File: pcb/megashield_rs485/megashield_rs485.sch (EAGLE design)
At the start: 20 parts, among them J11 DYNAMIXEL_RS485, U1 RS485

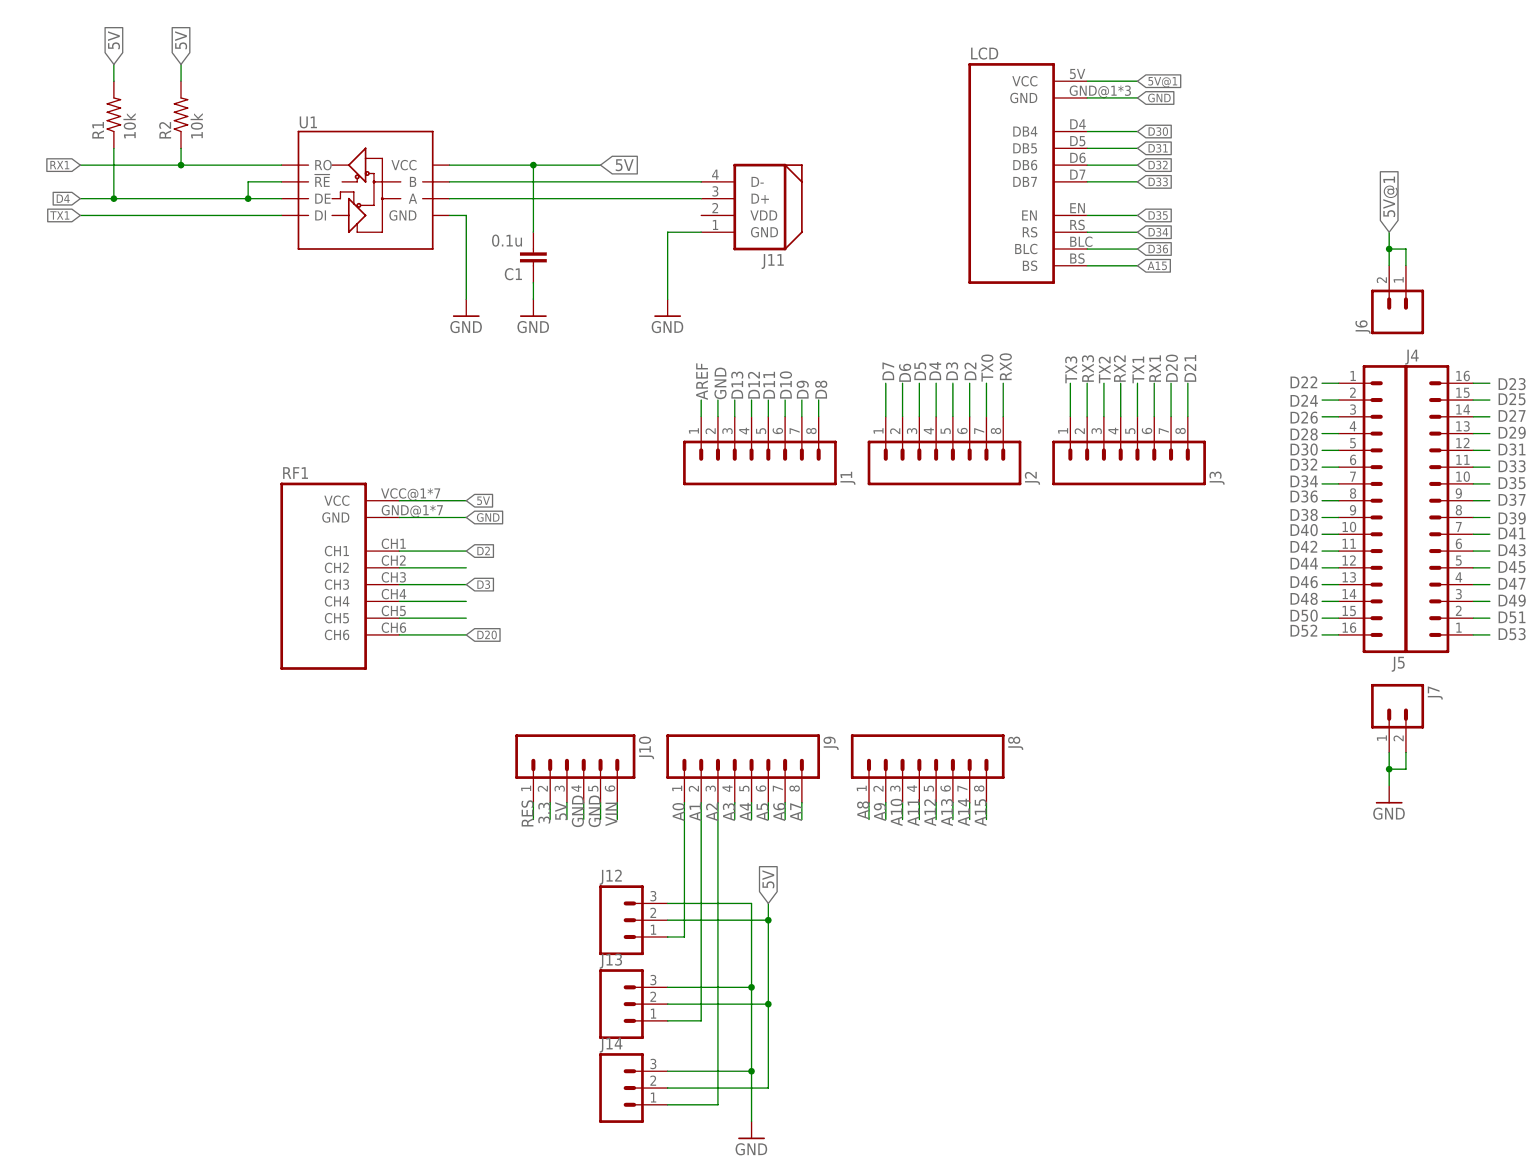
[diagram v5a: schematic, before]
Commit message: Add nRF24l01
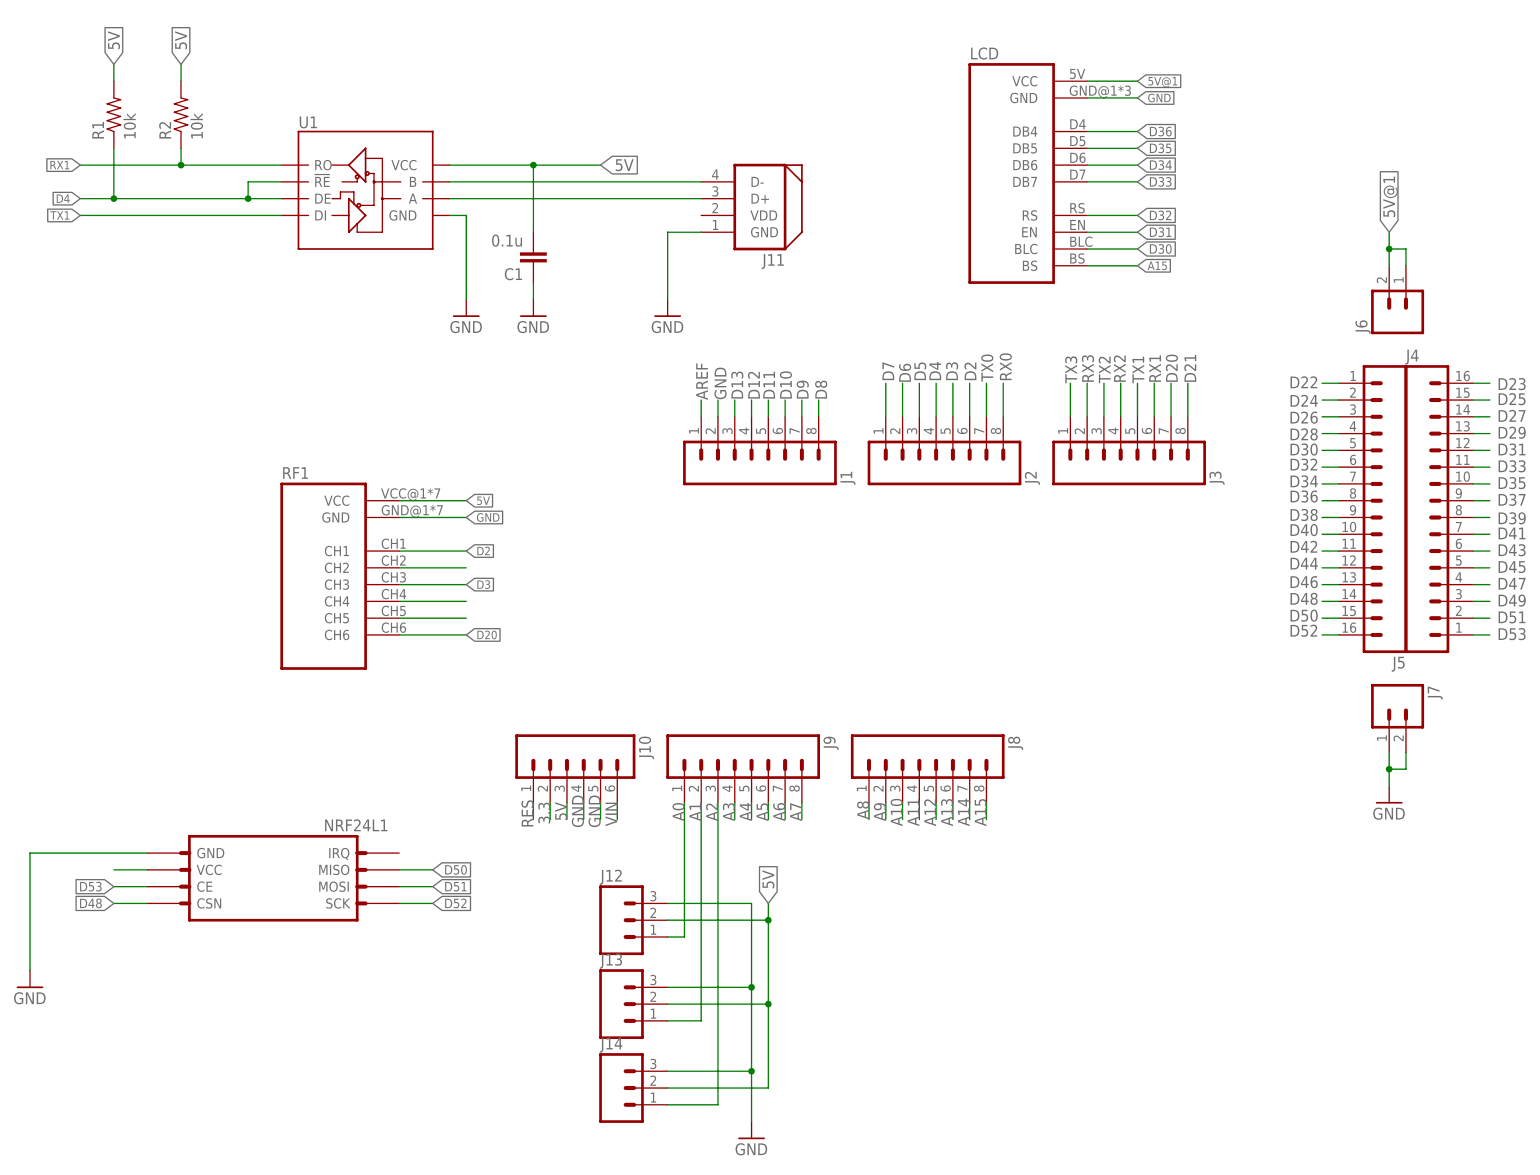
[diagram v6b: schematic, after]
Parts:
- added NRF24L1: (no value), mecatronica_eagle_lib:NRF
- J12, J13, J14: device mecatronica_eagle_lib:M03LONGPADS -> mecatronica_eagle_lib:M03PTH
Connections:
- new net N$10: NRF24L1.VCC
- net D30: now also LCD.BLC; no longer LCD.DB4
- net D31: now also LCD.EN; no longer LCD.DB5
- net D32: now also LCD.RS; no longer LCD.DB6
- net D34: now also LCD.DB6; no longer LCD.RS
- net D35: now also LCD.DB5; no longer LCD.EN
- net D36: now also LCD.DB4; no longer LCD.BLC
- net D48: now also NRF24L1.CSN
- net D50: now also NRF24L1.MISO
- net D51: now also NRF24L1.MOSI
- net D52: now also NRF24L1.SCK
- net D53: now also NRF24L1.CE
- net GND: now also NRF24L1.GND
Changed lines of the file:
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@@
 <?xml version="1.0" encoding="utf-8"?>
 <!DOCTYPE eagle SYSTEM "eagle.dtd">
-<eagle version="7.6.0">
+<eagle version="7.3.0">
 <drawing>
 <settings>
@@
 <part name="J11" library="mecatronica_eagle_lib" deviceset="DYNAMIXEL_RS485" device=""/>
 <part name="U1" library="mecatronica_eagle_lib" deviceset="SN75176B" device="" value="RS485"/>
-<part name="J12" library="mecatronica_eagle_lib" deviceset="M03" device="LONGPADS"/>
-<part name="J13" library="mecatronica_eagle_lib" deviceset="M03" device="LONGPADS"/>
-<part name="J14" library="mecatronica_eagle_lib" deviceset="M03" device="LONGPADS"/>
+<part name="J12" library="mecatronica_eagle_lib" deviceset="M03" device="PTH"/>
+<part name="J13" library="mecatronica_eagle_lib" deviceset="M03" device="PTH"/>
+<part name="J14" library="mecatronica_eagle_lib" deviceset="M03" device="PTH"/>
 <part name="GND1" library="SparkFun" deviceset="GND" device=""/>
 <part name="C1" library="mecatronica_eagle_lib" deviceset="CAP" device="PTH" value="0.1u"/>
@@
 <part name="GND5" library="SparkFun" deviceset="GND" device=""/>
 <part name="LCD" library="mecatronica_eagle_lib" deviceset="LCD_SHIELD" device=""/>
+<part name="NRF24L1" library="mecatronica_eagle_lib" deviceset="NRF" device=""/>
+<part name="GND6" library="SparkFun" deviceset="GND" device=""/>
 </parts>
 <sheets>
@@
 <instance part="GND5" gate="1" x="104.14" y="134.62"/>
 <instance part="LCD" gate="G$1" x="154.94" y="157.48"/>
+<instance part="NRF24L1" gate="G$1" x="58.42" y="50.8"/>
+<instance part="GND6" gate="1" x="7.62" y="33.02"/>
 </instances>
 <busses>
@@
 </segment>
 <segment>
-<wire x1="167.64" y1="162.56" x2="175.26" y2="162.56" width="0.1524" layer="91"/>
-<label x="175.26" y="162.56" size="1.27" layer="95" xref="yes"/>
-<pinref part="LCD" gate="G$1" pin="DB4"/>
+<pinref part="LCD" gate="G$1" pin="BLC"/>
+<wire x1="167.64" y1="144.78" x2="175.26" y2="144.78" width="0.1524" layer="91"/>
+<label x="175.26" y="144.78" size="1.4224" layer="95" xref="yes"/>
 </segment>
 </net>
@@
 </segment>
 <segment>
-<wire x1="167.64" y1="157.48" x2="175.26" y2="157.48" width="0.1524" layer="91"/>
-<label x="175.26" y="157.48" size="1.27" layer="95" xref="yes"/>
-<pinref part="LCD" gate="G$1" pin="DB6"/>
+<pinref part="LCD" gate="G$1" pin="RS"/>
+<wire x1="167.64" y1="149.86" x2="175.26" y2="149.86" width="0.1524" layer="91"/>
+<label x="175.26" y="149.86" size="1.4224" layer="95" xref="yes"/>
 </segment>
 </net>
@@
 </segment>
 <segment>
-<wire x1="167.64" y1="147.32" x2="175.26" y2="147.32" width="0.1524" layer="91"/>
-<label x="175.26" y="147.32" size="1.27" layer="95" xref="yes"/>
-<pinref part="LCD" gate="G$1" pin="RS"/>
+<pinref part="LCD" gate="G$1" pin="DB6"/>
+<wire x1="167.64" y1="157.48" x2="175.26" y2="157.48" width="0.1524" layer="91"/>
+<label x="175.26" y="157.48" size="1.4224" layer="95" xref="yes"/>
 </segment>
 </net>
@@
 </segment>
 <segment>
-<wire x1="167.64" y1="144.78" x2="175.26" y2="144.78" width="0.1524" layer="91"/>
-<label x="175.26" y="144.78" size="1.27" layer="95" xref="yes"/>
-<pinref part="LCD" gate="G$1" pin="BLC"/>
+<pinref part="LCD" gate="G$1" pin="DB4"/>
+<wire x1="167.64" y1="162.56" x2="175.26" y2="162.56" width="0.1524" layer="91"/>
+<label x="175.26" y="162.56" size="1.4224" layer="95" xref="yes"/>
 </segment>
 </net>
@@
 <pinref part="J5" gate="G$1" pin="14"/>
 </segment>
+<segment>
+<pinref part="NRF24L1" gate="G$1" pin="CSN"/>
+<wire x1="25.4" y1="45.72" x2="20.32" y2="45.72" width="0.1524" layer="91"/>
+<label x="20.32" y="45.72" size="1.4224" layer="95" rot="R180" xref="yes"/>
+</segment>
 </net>
 <net name="D50" class="0">
@@
 <pinref part="J5" gate="G$1" pin="15"/>
 </segment>
+<segment>
+<pinref part="NRF24L1" gate="G$1" pin="MISO"/>
+<wire x1="63.5" y1="50.8" x2="68.58" y2="50.8" width="0.1524" layer="91"/>
+<label x="68.58" y="50.8" size="1.4224" layer="95" xref="yes"/>
+</segment>
 </net>
 <net name="D52" class="0">
@@
 <pinref part="J5" gate="G$1" pin="16"/>
 </segment>
+<segment>
+<pinref part="NRF24L1" gate="G$1" pin="SCK"/>
+<wire x1="63.5" y1="45.72" x2="68.58" y2="45.72" width="0.1524" layer="91"/>
+<label x="68.58" y="45.72" size="1.4224" layer="95" xref="yes"/>
+</segment>
 </net>
 <net name="D25" class="0">
@@
 </segment>
 <segment>
-<wire x1="167.64" y1="160.02" x2="175.26" y2="160.02" width="0.1524" layer="91"/>
-<label x="175.26" y="160.02" size="1.27" layer="95" xref="yes"/>
-<pinref part="LCD" gate="G$1" pin="DB5"/>
+<pinref part="LCD" gate="G$1" pin="EN"/>
+<wire x1="167.64" y1="147.32" x2="175.26" y2="147.32" width="0.1524" layer="91"/>
+<label x="175.26" y="147.32" size="1.4224" layer="95" xref="yes"/>
 </segment>
 </net>
@@
 </segment>
 <segment>
+<pinref part="LCD" gate="G$1" pin="DB7"/>
 <wire x1="167.64" y1="154.94" x2="175.26" y2="154.94" width="0.1524" layer="91"/>
-<label x="175.26" y="154.94" size="1.27" layer="95" xref="yes"/>
-<pinref part="LCD" gate="G$1" pin="DB7"/>
+<label x="175.26" y="154.94" size="1.4224" layer="95" xref="yes"/>
 </segment>
 </net>
@@
 </segment>
 <segment>
-<wire x1="167.64" y1="149.86" x2="175.26" y2="149.86" width="0.1524" layer="91"/>
-<label x="175.26" y="149.86" size="1.27" layer="95" xref="yes"/>
-<pinref part="LCD" gate="G$1" pin="EN"/>
+<pinref part="LCD" gate="G$1" pin="DB5"/>
+<wire x1="167.64" y1="160.02" x2="175.26" y2="160.02" width="0.1524" layer="91"/>
+<label x="175.26" y="160.02" size="1.4224" layer="95" xref="yes"/>
 </segment>
 </net>
@@
 <pinref part="J4" gate="G$1" pin="2"/>
 </segment>
+<segment>
+<pinref part="NRF24L1" gate="G$1" pin="MOSI"/>
+<wire x1="63.5" y1="48.26" x2="68.58" y2="48.26" width="0.1524" layer="91"/>
+<label x="68.58" y="48.26" size="1.4224" layer="95" xref="yes"/>
+</segment>
 </net>
 <net name="D53" class="0">
@@
 <label x="234.188" y="87.376" size="1.778" layer="95" rot="R180"/>
 <pinref part="J4" gate="G$1" pin="1"/>
+</segment>
+<segment>
+<pinref part="NRF24L1" gate="G$1" pin="CE"/>
+<wire x1="25.4" y1="48.26" x2="20.32" y2="48.26" width="0.1524" layer="91"/>
+<label x="20.32" y="48.26" size="1.4224" layer="95" rot="R180" xref="yes"/>
 </segment>
 </net>
@@
 <pinref part="LCD" gate="G$1" pin="GND"/>
 </segment>
+<segment>
+<pinref part="NRF24L1" gate="G$1" pin="GND"/>
+<pinref part="GND6" gate="1" pin="GND"/>
+<wire x1="25.4" y1="53.34" x2="7.62" y2="53.34" width="0.1524" layer="91"/>
+<wire x1="7.62" y1="53.34" x2="7.62" y2="35.56" width="0.1524" layer="91"/>
+</segment>
 </net>
 <net name="N$4" class="0">
@@
 </segment>
 </net>
+<net name="N$10" class="0">
+<segment>
+<pinref part="NRF24L1" gate="G$1" pin="VCC"/>
+<wire x1="25.4" y1="50.8" x2="20.32" y2="50.8" width="0.1524" layer="91"/>
+</segment>
+</net>
